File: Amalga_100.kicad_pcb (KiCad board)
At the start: 6 copper layers, 268 x 155 mm, 198 parts, among them IC1 ADM3052, IC3 INA240A1, IC4 INA240A1, IC5 INA240A1, P1 USB_B, P2 Interface, P3 IN+, P4 IN-, P5 MOTOR3, P6 MOTOR2, P7 MOTOR1, P8 SWD, P9 CONN_6-HSWR-V2-rescue, Q1 IRFP4668PBF, Q10 IRFP4668PBF, Q11 IRFP4668PBF, Q12 IRFP4668PBF, Q13 Q_NPN_BCE, Q14 Q_PNP_BCE, Q15 Q_NPN_BCE, Q16 Q_PNP_BCE, Q2 IRFP4668PBF, Q3 IRFP4668PBF, Q4 IRFP4668PBF, Q5 IRFP4668PBF, Q6 IRFP4668PBF, Q7 IRFP4668PBF, Q8 IRFP4668PBF, Q9 IRFP4668PBF, U1 STM32F40X_LQFP64, U10 AD8664ARZ, U2 B1215S-2W, U3 JW5052C, U4 JW5052C, U5 ADUM3160, U6 AD2S1200YSTZ, U7 IRS2186, U8 IRS2186, U9 IRS2186, Y1 8MHz, Y2 8.912 MHZ

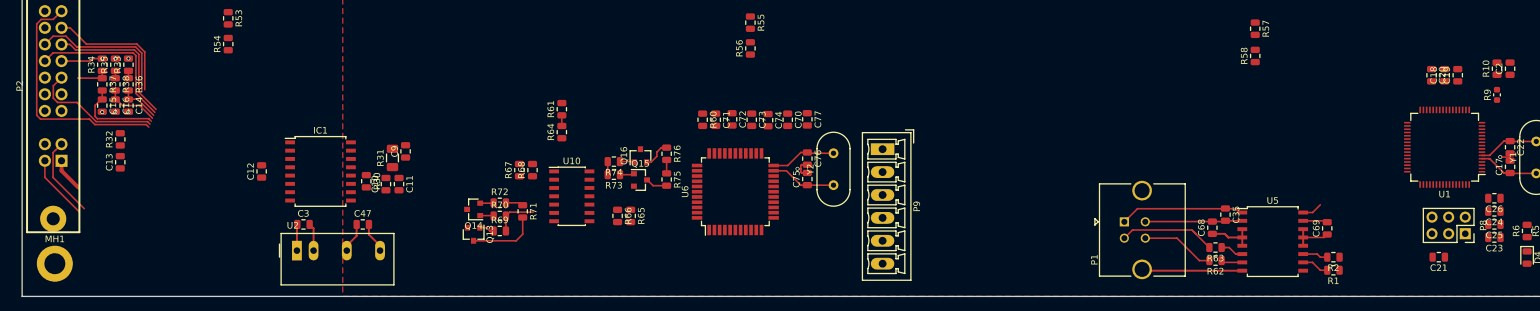
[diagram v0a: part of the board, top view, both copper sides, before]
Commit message: continued R2D AS1200 has encoder-interface
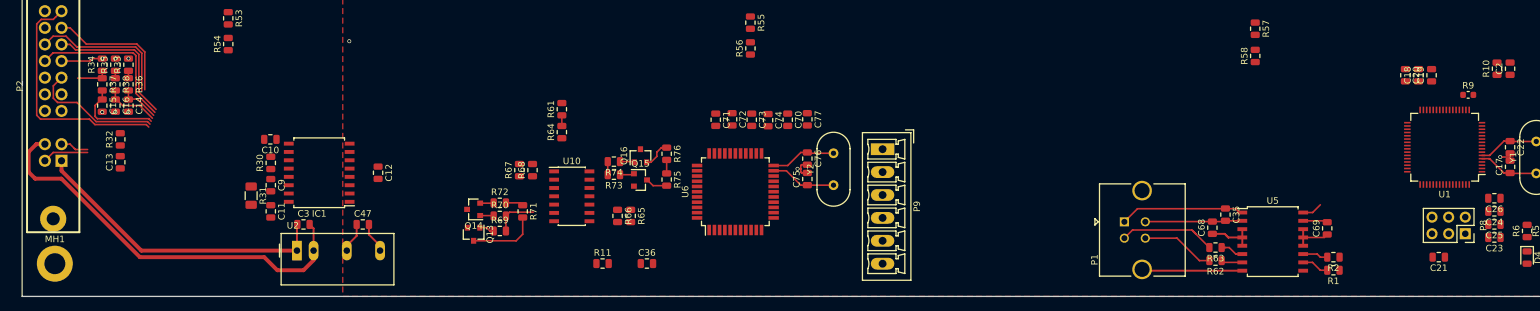
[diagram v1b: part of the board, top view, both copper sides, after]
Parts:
- removed R60: ?R, Resistor_SMD:R_0805_2012Metric
- added C36: 100nF, Capacitor_SMD:C_0805_2012Metric, F.Cu at (114.5, 187.0)
- added R11: , Resistor_SMD:R_0805_2012Metric, F.Cu at (107.7, 187.0)
- R61: value ?R -> 442R
- R64: value ?R -> 1K24
- moved R31 22.4 mm to (54.0, 176.6), turned to 270 degrees
- moved C9 21.2 mm to (57.0, 175.0), turned to 270 degrees
- moved C11 20.0 mm to (57.0, 179.0)
- moved C10 18.9 mm to (56.9, 168.0), turned to 180 degrees
- moved C12 17.8 mm to (73.4, 173.1), turned to 270 degrees
- moved R30 14.9 mm to (57.0, 171.6), turned to 90 degrees
- moved R9 4.40 mm to (240.0, 161.2), turned to 0 degrees
- moved C18 4.00 mm to (232.4, 158.2)
- moved C19 4.00 mm to (234.4, 158.2)
- moved C20 4.00 mm to (230.4, 158.2)
- moved IC1 0.28 mm to (64.4, 173.1), turned to 180 degrees
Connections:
- Q14 pad 2: Net-(Q14-Pad2) -> GND
- Q14 pad 3: GND -> Net-(Q14-Pad3)
- Q16 pad 2: Net-(Q16-Pad2) -> GND
- Q16 pad 3: GND -> Net-(Q16-Pad3)
- R72 pad 1: Net-(Q14-Pad2) -> Net-(Q14-Pad3)
- R76 pad 1: Net-(Q16-Pad2) -> Net-(Q16-Pad3)
- U1 pad 26: Net-(U1-Pad26) -> /Resolver/*CS
- U1 pad 27: Net-(U1-Pad27) -> /Resolver/*RDvel
- U1 pad 59: Net-(U1-Pad59) -> /Resolver/RD
- U10 pad 4: +12V -> +15V
- U6 pad 23: Net-(U6-Pad23) -> GND
- U6 pad 3: GND -> /Resolver/*CS
- U6 pad 5: Net-(R60-Pad1) -> /Resolver/*RDvel
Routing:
- net Earth: track 4.25 -> 62.2 mm
- net +12VA: track 9.19 -> 46.6 mm
- net GND: track 329.9 -> 353.8 mm, vias 18 -> 19
- net /CAN bus transceiver/CANL: track 12.4 -> 4.32 mm
- net /CAN bus transceiver/CANH: track 10.0 -> 7.05 mm
- net +BATT: track 120.9 -> 119.9 mm, vias 560 -> 563
- net (no net): vias 3 -> 0

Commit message: continued Resolver continued Routing
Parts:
- removed C14, C15, C16: 4n7, Capacitor_SMD:C_0805_2012Metric
- removed R33, R34, R35: 2k2, Resistor_SMD:R_0805_2012Metric
- removed R36, R37, R38: 10k, Resistor_SMD:R_0805_2012Metric
- added C37: 100nF, Capacitor_SMD:C_0805_2012Metric, F.Cu at (142.4, 178.7)
- added C38: 120pF, Capacitor_SMD:C_0805_2012Metric, F.Cu at (109.5, 184.1)
- added C40: 120pF, Capacitor_SMD:C_0805_2012Metric, F.Cu at (111.4, 170.4)
- added R12: 15k4, Resistor_SMD:R_0805_2012Metric, F.Cu at (111.5, 184.1)
- added R13: 15k4, Resistor_SMD:R_0805_2012Metric, F.Cu at (109.3, 170.4)
- C36: moved to B.Cu
- C74, C77: footprint Capacitor_SMD:C_0805_2012Metric -> Capacitor_Tantalum_SMD:CP_EIA-3216-12_Kemet-S
- L1, L2: footprint Inductors_SMD:L_Wuerth_MAPI-3020 -> Inductor_SMD:L_Taiyo-Yuden_NR-60xx
- Q13, Q15: value Q_NPN_BCE -> BC846B
- Q14, Q16: value Q_PNP_BCE -> BC856B
- U2: footprint Converters_DCDC_ACDC:DCDC-Conv_TRACO_TMR_1-xxxx_Single -> Converter_DCDC:Converter_DCDC_TRACO_TMR-1-xxxx_Single_THT
- moved R11 171.0 mm to (273.0, 143.1), turned to 270 degrees
- moved C1 85.4 mm to (11.1, 160.0)
- moved R3 85.4 mm to (8.00, 160.0)
- moved P9 65.7 mm to (87.5, 188.0), turned to 0 degrees
- moved Y2 54.6 mm to (93.0, 153.0), turned to 180 degrees
- moved C76 52.0 mm to (88.9, 157.0), turned to 0 degrees
- moved C75 49.9 mm to (92.1, 157.0), turned to 180 degrees
- moved C77 46.9 mm to (94.0, 178.0), turned to 0 degrees
- moved R61 44.8 mm to (144.7, 175.2)
- moved R64 44.8 mm to (144.7, 178.7)
- moved C70 44.6 mm to (94.0, 180.0), turned to 0 degrees
- moved R67 44.4 mm to (139.3, 175.2)
- moved R68 40.3 mm to (137.3, 175.2)
- moved C74 37.9 mm to (96.0, 157.0), turned to 0 degrees
- moved C73 35.2 mm to (95.8, 159.2), turned to 0 degrees
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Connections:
- C12 pad 2: Net-(C12-Pad2) -> GND
- IC1 pad 2: Net-(C12-Pad2) -> GND
- IC1 pad 3: Net-(IC1-Pad3) -> GND
- Q13 pad 2: +12V -> Net-(Q13-Pad2)
- Q13 pad 3: Net-(Q13-Pad3) -> +12V
- Q14 pad 2: GND -> Net-(Q14-Pad2)
- Q14 pad 3: Net-(Q14-Pad3) -> GND
- Q15 pad 2: +12V -> Net-(Q15-Pad2)
- Q15 pad 3: Net-(Q15-Pad3) -> +12V
- Q16 pad 2: GND -> Net-(Q16-Pad2)
- Q16 pad 3: Net-(Q16-Pad3) -> GND
- R71 pad 2: Net-(Q13-Pad3) -> Net-(Q13-Pad2)
- R72 pad 1: Net-(Q14-Pad3) -> Net-(Q14-Pad2)
- R75 pad 2: Net-(Q15-Pad3) -> Net-(Q15-Pad2)
- R76 pad 1: Net-(Q16-Pad3) -> Net-(Q16-Pad2)
- U1 pad 37: /MCU/HALL_1 -> A(enc)
- U1 pad 38: /MCU/HALL_2 -> B(enc)
- U1 pad 39: /MCU/HALL_3 -> NM(enc)
- U1 pad 40: Net-(U1-Pad40) -> dir(enc)
- U10 pad 13: /Resolver/R1 -> Net-(C38-Pad2)
- U10 pad 6: /Resolver/R2 -> Net-(C40-Pad2)
- U6 pad 25: Net-(U6-Pad25) -> A(enc)
- U6 pad 26: Net-(U6-Pad26) -> B(enc)
- U6 pad 27: Net-(U6-Pad27) -> NM(enc)
- U6 pad 28: Net-(U6-Pad28) -> dir(enc)
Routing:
- net Earth: track 62.2 -> 165.0 mm
- net /Resolver/Buffer Circuit R2D/*EXC: track 0.00 -> 55.9 mm, vias 0 -> 2
- net GND: track 353.8 -> 407.2 mm, vias 19 -> 17
- net Net-(P2-Pad19): track 36.4 -> 0.00 mm
- net +12VA: track 46.6 -> 83.0 mm
- net /CAN bus transceiver/CANL: track 4.32 -> 37.6 mm
- net /CAN bus transceiver/CANH: track 7.05 -> 38.9 mm
- net Net-(C40-Pad2): track 0.00 -> 31.5 mm
- net Net-(R73-Pad2): track 2.00 -> 32.5 mm
- net /Resolver/R2: track 2.71 -> 31.4 mm
- net Net-(C38-Pad2): track 0.00 -> 27.1 mm
- net +12V: track 0.00 -> 25.9 mm
- net /MCU/SCK_ADC_EXT: track 24.5 -> 0.00 mm
- net /MCU/RX_SDA_NSS: track 22.2 -> 0.00 mm
- net /MCU/TX_SCL_MOSI: track 21.9 -> 0.00 mm
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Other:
- board text added: "Cos"
- board text added: "CosLo"
- board text added: "PWR"
- board text added: "R1"
- board text added: "R2"
- board text added: "Resolver"
- board text added: "Sin"
- board text added: "SinLo"
- board text added: "gain1 = - R1/R2 gain2 = - R3/R4"

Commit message: continued routing, almost finished resolver. todo: -calc resistors for gain (resolver)       -Anfahren ohne encoder signal?!       -12V buffer R2D
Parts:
- moved R39 208.7 mm to (69.6, 154.4), turned to 270 degrees
- moved C4 201.2 mm to (73.1, 154.9), turned to 180 degrees
- moved U3 201.2 mm to (73.1, 154.9), turned to 180 degrees
- moved C6 200.6 mm to (73.1, 157.9), turned to 0 degrees
- moved L1 195.7 mm to (75.5, 162.4), turned to 180 degrees
- moved R42 193.3 mm to (77.1, 154.9), turned to 90 degrees
- moved C8 190.7 mm to (78.1, 157.9), turned to 0 degrees
- moved R41 189.3 mm to (79.1, 154.9), turned to 270 degrees
- moved P8 71.9 mm to (167.6, 182.0)
- moved C21 71.5 mm to (164.0, 185.0)
- moved C26 70.0 mm to (163.0, 172.0), turned to 90 degrees
- moved C24 68.7 mm to (165.0, 157.0), turned to 0 degrees
- moved C17 65.6 mm to (180.9, 168.7)
- moved C19 65.6 mm to (160.5, 168.4)
- moved C20 65.6 mm to (179.5, 162.4)
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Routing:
- net +15V: track 208.2 -> 533.5 mm, vias 6 -> 9
- net +3V3: track 161.4 -> 455.5 mm, vias 3 -> 8
- net +5V: track 29.8 -> 193.0 mm, vias 1 -> 4
- net NM(enc): track 0.00 -> 79.5 mm, vias 0 -> 2
- net A(enc): track 0.00 -> 79.1 mm, vias 0 -> 2
- net dir(enc): track 0.00 -> 78.4 mm, vias 0 -> 2
- net B(enc): track 0.00 -> 78.3 mm, vias 0 -> 2
- net /Resolver/RD: track 0.00 -> 48.5 mm
- net /Resolver/*CS: track 0.00 -> 48.3 mm
- net SPI1_MOSI(R2D): track 0.00 -> 48.2 mm
- net /Resolver/*RDvel: track 0.00 -> 48.0 mm
- net SPI1_SCK(R2D): track 0.00 -> 48.0 mm
- net SPI1_MISO(R2D): track 0.00 -> 47.6 mm
- net GND: track 407.2 -> 427.3 mm, vias 17 -> 19
- net /Resolver/Buffer Circuit R2D/*EXC: track 55.9 -> 38.8 mm
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- removed copper zone on inner_layer1, net +15V

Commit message: Nearly Finished Layout. R2D 12V.
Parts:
- added C42: 1u, Capacitor_SMD:C_0805_2012Metric, B.Cu at (175.9, 168.0)
- C19, C20, C23, C24, C25, C26: moved to B.Cu
- moved R53 136.0 mm to (186.4, 155.8)
- moved R54 136.0 mm to (186.4, 158.9)
- moved R9 62.2 mm to (175.5, 156.2), turned to 270 degrees
- moved R55 57.8 mm to (189.7, 155.8), turned to 270 degrees
- moved R5 57.3 mm to (191.2, 183.2)
- moved D3 57.3 mm to (191.2, 186.8)
- moved R6 56.8 mm to (188.7, 183.2)
- moved D4 56.8 mm to (188.7, 186.8)
- moved C2 56.5 mm to (178.1, 158.0), turned to 0 degrees
- moved R10 55.8 mm to (178.1, 156.0), turned to 0 degrees
- moved R56 54.5 mm to (189.7, 158.8), turned to 90 degrees
- moved R57 15.5 mm to (192.7, 155.9)
- moved R58 15.2 mm to (192.7, 158.9)
- moved C35 8.00 mm to (220.1, 185.4)
- moved C68 8.00 mm to (222.1, 183.4)
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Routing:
- net /MCU/SERVO: track 0.00 -> 174.5 mm, vias 0 -> 2
- net /MCU/RX_SDA_NSS: track 0.00 -> 174.1 mm, vias 0 -> 1
- net /MCU/SCK_ADC_EXT: track 0.00 -> 164.3 mm, vias 0 -> 1
- net /MCU/TX_SCL_MOSI: track 0.00 -> 158.4 mm, vias 0 -> 1
- net /Filters/TEMP_IN: track 0.00 -> 157.9 mm, vias 0 -> 2
- net /MCU/MISO_ADC_EXT2: track 0.00 -> 154.5 mm, vias 0 -> 1
- net +3V3: track 455.5 -> 595.4 mm, vias 8 -> 14
- net /MCU/H3_pwm: track 63.7 -> 189.8 mm, vias 1 -> 2
- net H3_VS: track 93.5 -> 218.4 mm, vias 46 -> 47
- net /MCU/U_Bat: track 1.78 -> 124.0 mm, vias 0 -> 2
- net /MCU/L3_pwm: track 61.0 -> 181.5 mm, vias 1 -> 2
- net /MCU/BR_SO1: track 37.3 -> 149.9 mm, vias 1 -> 2
- net /CAN bus transceiver/CAN_TX: track 0.00 -> 110.9 mm, vias 0 -> 2
- net /CAN bus transceiver/CAN_RX: track 0.00 -> 107.2 mm, vias 0 -> 2
- net /MCU/CAN_VSS_Sense: track 0.00 -> 101.7 mm, vias 0 -> 2
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- added copper zone on B.Cu, net +3V3
- added copper zone on B.Cu, net GND
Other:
- board text added: "+12V"
- board text added: "CANH"
- board text added: "CANL"
- board text added: "GNDC"
- board text added: "Status"

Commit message: moved silkscreen values
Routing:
- net GND: track 457.0 -> 463.2 mm
- net +BATT: vias 563 -> 562
- added copper zone on inner_layer1, net GND
- added copper zone on inner_layer2, net GND
- added copper zone on inner_layer3_(GND), net GND
- added copper zone on inner_layer4_(Sig), net GND

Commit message: started with some changes. Whats to do: -R2D to 15V. -Hall-Filter -GND-decoupling by aperiodic caps -calculate R2D-Buffer gain -R2D gain semi switchable -frequency R2D switchable
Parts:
- removed R11: , Resistor_SMD:R_0805_2012Metric
- added C14: 4n7, Capacitor_SMD:C_0805_2012Metric, F.Cu at (48.4, 157.8)
- added C15: 4n7, Capacitor_SMD:C_0805_2012Metric, F.Cu at (48.4, 159.8)
- added C16: 4n7, Capacitor_SMD:C_0805_2012Metric, F.Cu at (45.0, 159.8)
- added NT1: Net-Tie_2, NetTie:NetTie-2_SMD_Pad2.0mm, F.Cu at (272.9, 143.5)
- added R33: 2k2, Resistor_SMD:R_0805_2012Metric, F.Cu at (41.6, 155.9)
- added R34: 2k2, Resistor_SMD:R_0805_2012Metric, F.Cu at (41.6, 159.8)
- added R35: 2k2, Resistor_SMD:R_0805_2012Metric, F.Cu at (45.0, 155.9)
- added R36: 10k, Resistor_SMD:R_0805_2012Metric, F.Cu at (48.4, 155.9)
- added R37: 10k, Resistor_SMD:R_0805_2012Metric, F.Cu at (45.0, 157.8)
- added R38: 10k, Resistor_SMD:R_0805_2012Metric, F.Cu at (41.6, 157.8)
- moved D2 83.4 mm to (184.8, 186.5)
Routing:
- net GNDPWR: track 48.9 -> 69.6 mm, vias 940 -> 938
- net GND: track 463.2 -> 457.0 mm, vias 27 -> 48
- net /MCU/LED_GREEN: track 32.9 -> 31.5 mm
- net +3V3: track 595.4 -> 596.6 mm
- net /USB-Isolator/UD-: track 15.3 -> 14.6 mm

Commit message: -added some more caps espacially decoupling-caps -little changes
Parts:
- added C45: 100n, Capacitor_SMD:C_0805_2012Metric, F.Cu at (72.0, 144.6)
- added C46: 100n, Capacitor_SMD:C_0805_2012Metric, F.Cu at (109.0, 144.6)
- added C48: 100n, Capacitor_SMD:C_0805_2012Metric, F.Cu at (57.5, 144.6)
- added C49: 1u 600V, Capacitor_SMD:C_2220_5650Metric, F.Cu at (212.4, 78.2)
- added C59: 1u 600V, Capacitor_SMD:C_2220_5650Metric, F.Cu at (135.4, 78.2)
- added C60: 1u 600V, Capacitor_SMD:C_2220_5650Metric, F.Cu at (58.4, 78.2)
- added C61: 1u 600V, Capacitor_SMD:C_2220_5650Metric, B.Cu at (263.0, 78.5)
- added C63: 1u 600V, Capacitor_SMD:C_2220_5650Metric, B.Cu at (277.0, 78.5)
- added C78: 1u 600V, Capacitor_SMD:C_2220_5650Metric, B.Cu at (284.0, 78.5)
- added JP1: SolderJumper_3_Bridged12, Jumper:SolderJumper-3_P1.3mm_Bridged12_RoundedPad1.0x1.5mm, F.Cu at (82.9, 168.6)
- added JP2: SolderJumper_3_Bridged12, Jumper:SolderJumper-3_P1.3mm_Bridged12_RoundedPad1.0x1.5mm, F.Cu at (83.0, 166.4)
- added JP3: SolderJumper_3_Bridged12, Jumper:SolderJumper-3_P1.3mm_Bridged12_RoundedPad1.0x1.5mm, F.Cu at (82.9, 164.2)
- R16, R22, R28: moved to B.Cu
- moved R4 82.7 mm to (185.9, 183.3)
- moved R36 11.3 mm to (39.6, 163.0)
- moved R35 8.97 mm to (36.5, 158.7), turned to 180 degrees
- moved R33 8.73 mm to (36.6, 163.0), turned to 180 degrees
- moved C14 7.69 mm to (42.7, 163.0)
- moved R37 6.26 mm to (39.6, 160.9)
- moved C15 5.90 mm to (42.6, 160.9)
- moved R34 5.23 mm to (36.5, 160.9), turned to 180 degrees
- moved C16 2.61 mm to (42.6, 158.7)
- moved R38 2.25 mm to (39.5, 158.7)
- moved R16 2.19 mm to (208.0, 70.8)
- moved R28 1.94 mm to (54.2, 70.8)
- moved R22 1.56 mm to (131.7, 70.8)
- moved D2 1.13 mm to (185.9, 186.8)
- moved L1 0.89 mm to (76.3, 162.2)
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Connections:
- P2 pad 10: Net-(P2-Pad10) -> /Filters/HALL1_IN
- P2 pad 8: Net-(P2-Pad8) -> /Filters/HALL3_IN
- P2 pad 9: Net-(P2-Pad9) -> /Filters/HALL2_IN
- U1 pad 37: A(enc) -> /MCU/HALL_1
- U1 pad 38: B(enc) -> /MCU/HALL_2
- U1 pad 39: NM(enc) -> /MCU/HALL_3
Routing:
- net /MCU/HALL_1: track 0.00 -> 84.5 mm, vias 0 -> 2
- net /MCU/HALL_3: track 0.00 -> 84.3 mm, vias 0 -> 2
- net /MCU/HALL_2: track 0.00 -> 83.4 mm, vias 0 -> 2
- net B(enc): track 78.2 -> 3.85 mm, vias 2 -> 0
- net A(enc): track 78.6 -> 4.53 mm, vias 2 -> 0
- net NM(enc): track 78.6 -> 4.53 mm, vias 2 -> 0
- net /Filters/HALL1_OUT: track 0.00 -> 51.0 mm
- net /Filters/HALL2_OUT: track 0.00 -> 45.8 mm
- net /Filters/HALL3_OUT: track 0.00 -> 44.7 mm
- net H3_VS: track 218.4 -> 250.2 mm, vias 47 -> 46
- net H2_VS: track 146.5 -> 174.6 mm, vias 48 -> 47
- net /Filters/HALL1_IN: track 0.00 -> 25.3 mm
- net +3V3: track 596.6 -> 619.2 mm
- net /Filters/HALL3_IN: track 0.00 -> 19.8 mm
- net /Filters/HALL2_IN: track 0.00 -> 18.2 mm
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- removed copper zone on B.Cu, net /Mosfet driver/H3_LOW
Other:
- net class HV: clearance 3 -> 2
- board text added: "B+"
- board text added: "B-"
- board text added: "Hall|Enc"
- board text added: "Prog/ SWD"
- board text added: "Software"
- board text added: "config"

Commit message: Mäusepiano (for Piano-Beginner) Areas tidied up new Phase- and Batterie-Connector and Benchmark for Pressfit Hall-filter back on PCB solder-jumper for choice: Resolver or Hallfilter
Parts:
- added P10: IN-, eigene_mod:redcube_250A_2, F.Cu at (29.1, 125.0)
- added R11: 1Meg, Resistors_SMD:R_0805, F.Cu at (209.5, 187.9)
- added R18: 10k, Resistors_SMD:R_0805, F.Cu at (100.0, 159.2)
- added SW1: SW_DIP_x02, Buttons_Switches_SMD:SW_DIP_x2_W5.08mm_Slide_Copal_CHS-A, F.Cu at (82.8, 177.4)
- added SYM1: SYM_ESD_Small, Symbols:ESD-Logo_13.2x12mm_SilkScreen, F.Cu at (127.5, 155.0)
- added SYM2: SYM_Arrow45_Tiny, Symbols:Symbol_Attention_CopperTop_Small, F.Cu at (215.0, 165.0)
- L1, L2: footprint Inductor_SMD:L_Taiyo-Yuden_NR-60xx -> Inductors_SMD:L_Wuerth_MAPI-3020
- P3, P4, P5, P6, P7: footprint eigene_mod:redcube_250A_2 -> Mounting_Holes:MountingHole_5mm_Pad_Via
- moved P4 3.16 mm to (29.0, 107.0)
- moved D12 0.70 mm to (139.3, 60.1)
- moved D8 0.48 mm to (165.6, 60.4)
- moved Q6 0.46 mm to (172.6, 102.4)
- moved Q3 0.36 mm to (213.9, 64.0)
- moved Q5 0.20 mm to (163.2, 64.0)
- moved Q7 0.17 mm to (137.2, 64.0)
- moved Q9 0.14 mm to (85.7, 64.1)
- moved Q12 0.10 mm to (95.9, 102.5)
- moved Q11 0.10 mm to (59.6, 64.0)
- moved Q8 0.09 mm to (142.0, 100.0)
- moved Q2 0.09 mm to (249.9, 102.5)
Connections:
- C59 pad 2: Net-(C59-Pad2) -> /Mosfet driver/H2_LOW
- C60 pad 2: Net-(C60-Pad2) -> /Mosfet driver/H3_LOW
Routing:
- net +BATT: track 129.2 -> 74.8 mm, vias 563 -> 565
- net H2_VS: track 174.6 -> 143.6 mm
- net H3_VS: track 250.2 -> 221.4 mm
- net /Resolver/*RDvel: track 76.6 -> 93.2 mm
- net /USB-Isolator/GND1: track 45.1 -> 55.0 mm
- net Net-(SW1-Pad2): track 0.00 -> 9.37 mm
- net Net-(SW1-Pad1): track 0.00 -> 7.75 mm
- net +5V: track 202.6 -> 210.2 mm
- net GND: track 447.2 -> 452.6 mm
- net Net-(C6-Pad1): track 8.37 -> 13.2 mm
- net Net-(C7-Pad1): track 6.21 -> 8.37 mm
- net +3V3: track 619.2 -> 620.7 mm
- net Net-(C60-Pad2): vias 1 -> 0
- net Net-(C59-Pad2): vias 1 -> 0
- net GNDPWR: vias 939 -> 931
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- added copper zone on inner_layer1, net /Mosfet driver/H1_LOW
- added copper zone on inner_layer2, net /Mosfet driver/H1_LOW
- added copper zone on inner_layer3_(GND), net /Mosfet driver/H1_LOW
- added copper zone on inner_layer4_(Sig), net /Mosfet driver/H1_LOW
- added copper zone on B.Cu, net /Mosfet driver/H3_LOW
- added copper zone on inner_layer1, net /Mosfet driver/H3_LOW
- added copper zone on inner_layer2, net /Mosfet driver/H3_LOW
- added copper zone on inner_layer3_(GND), net /Mosfet driver/H3_LOW
- added copper zone on inner_layer4_(Sig), net /Mosfet driver/H3_LOW
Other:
- board text added: "prim. to sec. Ohm 1:1 100k 2:1 40k 5:1 10k"
- board text removed: "gain1 = - R1/R2 gain2 = - R3/R4"
